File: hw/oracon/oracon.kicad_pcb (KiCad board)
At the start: 2 copper layers, 81 x 56 mm, 108 parts, among them J2 SIM_Card, J3 USB_A, J4 Conn_Coaxial, J5 USB_C_Receptacle_USB2.0_16P, Q1 SS8050, Q2 SS8050, Q3 SS8050, Q5 SS8050, SW1 SW_Push, U1 TP5100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

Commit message: Further routing
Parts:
- moved R10 1.75 mm to (3.42, 101.1)
- moved R11 1.75 mm to (2.44, 101.1)
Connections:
- U3 pad 11: unconnected-(U3-IO7-Pad11) -> LED1_B
- U3 pad 12: unconnected-(U3-IO8-Pad12) -> LED1_G
- U3 pad 13: unconnected-(U3-IO9-Pad13) -> LED1_R
- U3 pad 16: unconnected-(U3-IO12-Pad16) -> SI_TX
- U3 pad 17: unconnected-(U3-IO13-Pad17) -> SI_RX
- U3 pad 18: SI_TX -> ADC_BATT
- U3 pad 19: SI_RX -> NBIOT_TX
- U3 pad 20: ADC_BATT -> NBIOT_RX
- U3 pad 21: NBIOT_TX -> CHG_STAT
- U3 pad 22: NBIOT_RX -> STBY_STAT
- U3 pad 23: CHG_STAT -> unconnected-(U3-IO19-Pad23)
- U3 pad 24: STBY_STAT -> unconnected-(U3-IO20-Pad24)
- U3 pad 25: LED1_B -> unconnected-(U3-IO21-Pad25)
- U3 pad 26: LED1_G -> unconnected-(U3-IO26-Pad26)
- U3 pad 27: LED1_R -> unconnected-(U3-IO47-Pad27)
- U3 pad 28: LED3_R -> unconnected-(U3-IO33-Pad28)
- U3 pad 29: LED3_G -> unconnected-(U3-IO34-Pad29)
- U3 pad 30: LED3_B -> unconnected-(U3-IO48-Pad30)
- U3 pad 31: LED2_R -> unconnected-(U3-IO35-Pad31)
- U3 pad 32: LED2_G -> unconnected-(U3-IO36-Pad32)
- U3 pad 33: LED2_B -> LED3_R
- U3 pad 34: unconnected-(U3-IO38-Pad34) -> LED3_G
- U3 pad 35: unconnected-(U3-IO39-Pad35) -> LED3_B
- U3 pad 36: unconnected-(U3-IO40-Pad36) -> LED2_R
- U3 pad 37: unconnected-(U3-IO41-Pad37) -> LED2_G
- U3 pad 38: unconnected-(U3-IO42-Pad38) -> LED2_B
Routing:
- net LED1_R: track 49.3 -> 57.2 mm
- net LED3_R: track 29.9 -> 22.6 mm
- net LED1_G: track 49.7 -> 56.0 mm
- net LED3_G: track 28.9 -> 23.0 mm
- net LED2_R: track 47.8 -> 42.6 mm
- net LED1_B: track 50.6 -> 55.4 mm
- net LED3_B: track 27.9 -> 23.5 mm
- net LED2_B: track 47.6 -> 43.2 mm
- net LED2_G: track 47.1 -> 42.7 mm
- net PC_RX: track 38.9 -> 41.5 mm
- net PC_TX: track 40.0 -> 42.1 mm
- net VCC: track 42.6 -> 41.0 mm
- net SI_TX: track 22.0 -> 23.5 mm
- net SI_RX: track 19.3 -> 20.6 mm
- net NBIOT_RX: track 43.6 -> 44.5 mm
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
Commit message: Moved charging LED to green channel
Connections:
- D5 pad 2: unconnected-(D5-GK-Pad2) -> Net-(D5-GK)
- D5 pad 3: Net-(D5-BK) -> unconnected-(D5-BK-Pad3)
- R25 pad 2: Net-(D5-BK) -> Net-(D5-GK)
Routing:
- net Net-(D5-BK): track 3.95 -> 0.00 mm
- net Net-(D5-GK): track 0.00 -> 2.51 mm
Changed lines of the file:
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@@
 	(net 79 "LED3_R")
 	(net 80 "VCC")
-	(net 81 "Net-(D5-BK)")
-	(net 82 "unconnected-(D5-GK-Pad2)")
+	(net 81 "unconnected-(D5-BK-Pad3)")
+	(net 82 "Net-(D5-GK)")
 	(net 83 "Net-(D5-RK)")
 	(net 84 "unconnected-(U3-IO5-Pad9)")
@@
 			(size 1.5 1)
 			(layers "F.Cu" "F.Mask" "F.Paste")
-			(net 82 "unconnected-(D5-GK-Pad2)")
+			(net 82 "Net-(D5-GK)")
 			(pinfunction "GK")
 			(pintype "passive")
@@
 			(size 1.5 1)
 			(layers "F.Cu" "F.Mask" "F.Paste")
-			(net 81 "Net-(D5-BK)")
+			(net 81 "unconnected-(D5-BK-Pad3)")
 			(pinfunction "BK")
 			(pintype "passive")
@@
 			(layers "F.Cu" "F.Mask" "F.Paste")
 			(roundrect_rratio 0.25)
-			(net 81 "Net-(D5-BK)")
+			(net 82 "Net-(D5-GK)")
 			(pintype "passive")
 		)
@@
 		)
 	)
+	(dimension
+		(type orthogonal)
+		(layer "Cmts.User")
+		(pts
+			(xy 44.700001 107.6) (xy 44.700001 51.599999)
+		)
+		(height 15.609999)
+		(orientation 1)
+		(format
+			(prefix "")
+			(suffix "")
+			(units 3)
+			(units_format 1)
+			(precision 4)
+		)
+		(style
+			(thickness 0.1)
+			(arrow_length 1.27)
+			(text_position_mode 0)
+			(arrow_direction outward)
+			(extension_height 0.58642)
+			(extension_offset 0.5)
+			(keep_text_aligned yes)
+		)
+		(gr_text "56,0000 mm"
+			(at 59.16 79.599999 90)
+			(layer "Cmts.User")
+			(effects
+				(font
+					(size 1 1)
+					(thickness 0.15)
+				)
+			)
+		)
+	)
+	(dimension
+		(type orthogonal)
+		(layer "Cmts.User")
+		(pts
+			(xy -9.66 79.74) (xy 44.66 85.02)
+		)
+		(height -38.17)
+		(orientation 0)
+		(format
+			(prefix "")
+			(suffix "")
+			(units 3)
+			(units_format 1)
+			(precision 4)
+		)
+		(style
+			(thickness 0.1)
+			(arrow_length 1.27)
+			(text_position_mode 0)
+			(arrow_direction outward)
+			(extension_height 0.58642)
+			(extension_offset 0.5)
+			(keep_text_aligned yes)
+		)
+		(gr_text "54,3200 mm"
+			(at 17.5 40.42 0)
+			(layer "Cmts.User")
+			(effects
+				(font
+					(size 1 1)
+					(thickness 0.15)
+				)
+			)
+		)
+	)
 	(via
 		(at 24.27 81.58)
@@
 	)
 	(segment
-		(start -31.55 90.5)
-		(end -29.26 92.79)
+		(start -31.54 94.01)
+		(end -31.55 94)
+		(width 0.2)
+		(layer "F.Cu")
+		(net 82)
+	)
+	(segment
+		(start -29.26 93.5)
+		(end -29.77 94.01)
 		(width 0.2)
 		(layer "F.Cu")
-		(net 81)
+		(net 82)
 	)
 	(segment
-		(start -29.26 92.79)
-		(end -29.26 93.5)
+		(start -29.77 94.01)
+		(end -31.54 94.01)
 		(width 0.2)
 		(layer "F.Cu")
-		(net 81)
+		(net 82)
+	)
+	(segment
+		(start -32.849 95.051)
+		(end -32.95 94.95)
+		(width 0.2)
+		(layer "F.Cu")
+		(net 83)
 	)
 	(segment
-		(start -32.95 93.548)
-		(end -32.351 92.949)
+		(start -32.95 94.95)
+		(end -32.95 94)
 		(width 0.2)
 		(layer "F.Cu")
@@
 	)
 	(segment
-		(start -32.351 92.949)
-		(end -30.801 92.949)
+		(start -29.801 95.051)
+		(end -32.849 95.051)
 		(width 0.2)
 		(layer "F.Cu")
@@
 	)
 	(segment
-		(start -30.801 92.949)
-		(end -29.25 94.5)
+		(start -29.25 94.5)
+		(end -29.801 95.051)
 		(width 0.2)
 		(layer "F.Cu")

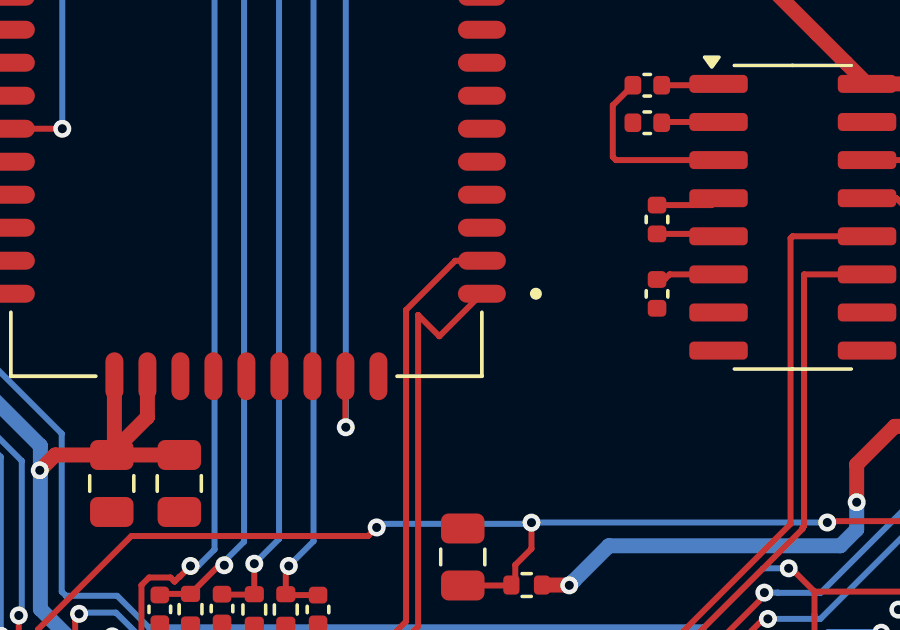
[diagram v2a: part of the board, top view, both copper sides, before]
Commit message: Unconnected schema fix
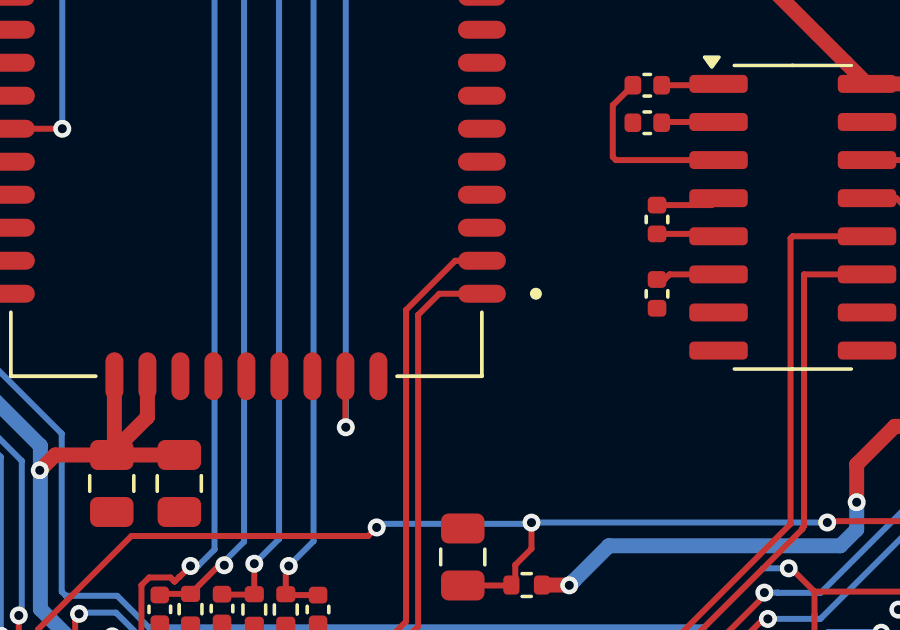
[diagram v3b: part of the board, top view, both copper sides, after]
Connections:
- U7 pad 12: Net-(U7-~{WAKEUP}-Pad12) -> unconnected-(U7-~{WAKEUP}-Pad12)_1
- U7 pad 39: Net-(U7-~{WAKEUP}-Pad12) -> unconnected-(U7-~{WAKEUP}-Pad12)
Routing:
- net NBIOT_RX: track 44.5 -> 44.0 mm
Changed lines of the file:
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@@
 	(net 102 "unconnected-(U7-RESERVED-Pad9)")
 	(net 103 "unconnected-(U7-UART0_RXD-Pad23)")
-	(net 104 "Net-(U7-~{WAKEUP}-Pad12)")
+	(net 104 "unconnected-(U7-~{WAKEUP}-Pad12)")
 	(net 105 "unconnected-(U7-UART1_DCD-Pad5)")
 	(net 106 "Net-(Q3-C)")
@@
 	(net 132 "unconnected-(U3-IO20-Pad24)")
 	(net 133 "unconnected-(U3-IO19-Pad23)")
+	(net 134 "unconnected-(U7-~{WAKEUP}-Pad12)_1")
 	(footprint "TestPoint:TestPoint_Pad_D1.5mm"
 		(layer "F.Cu")
@@
 			(net 12 "unconnected-(J5-SBU1-PadA8)")
 			(pinfunction "SBU1")
-			(pintype "bidirectional")
+			(pintype "bidirectional+no_connect")
 		)
 		(pad "B5" smd rect
@@
 			(net 11 "unconnected-(J5-SBU2-PadB8)")
 			(pinfunction "SBU2")
-			(pintype "bidirectional")
+			(pintype "bidirectional+no_connect")
 		)
 		(pad "S1" thru_hole oval
@@
 			(net 96 "unconnected-(J2-VPP-Pad6)")
 			(pinfunction "VPP")
-			(pintype "input")
+			(pintype "input+no_connect")
 			(thermal_bridge_angle 45)
 		)
@@
 			(net 97 "unconnected-(U7-UART1_RTS-Pad3)")
 			(pinfunction "UART1_RTS")
-			(pintype "input")
+			(pintype "input+no_connect")
 			(solder_mask_margin 0.102)
 		)
@@
 			(net 92 "unconnected-(U7-UART1_CTS-Pad4)")
 			(pinfunction "UART1_CTS")
-			(pintype "output")
+			(pintype "output+no_connect")
 			(solder_mask_margin 0.102)
 		)
@@
 			(net 105 "unconnected-(U7-UART1_DCD-Pad5)")
 			(pinfunction "UART1_DCD")
-			(pintype "output")
+			(pintype "output+no_connect")
 			(solder_mask_margin 0.102)
 		)
@@
 			(net 88 "unconnected-(U7-UART1_DTR-Pad6)")
 			(pinfunction "UART1_DTR")
-			(pintype "input")
+			(pintype "input+no_connect")
 			(solder_mask_margin 0.102)
 		)
@@
 			(net 94 "unconnected-(U7-UART1_RI-Pad7)")
 			(pinfunction "UART1_RI")
-			(pintype "output")
+			(pintype "output+no_connect")
 			(solder_mask_margin 0.102)
 		)
@@
 			(net 108 "unconnected-(U7-BOOT-Pad10)")
 			(pinfunction "BOOT")
-			(pintype "input")
+			(pintype "input+no_connect")
 			(solder_mask_margin 0.102)
 		)
@@
 			(net 109 "unconnected-(U7-AON_GPIO-Pad11)")
 			(pinfunction "AON_GPIO")
-			(pintype "bidirectional")
+			(pintype "bidirectional+no_connect")
 			(solder_mask_margin 0.102)
 		)
@@
 			(size 1.6 0.6)
 			(layers "F.Cu" "F.Mask" "F.Paste")
-			(net 104 "Net-(U7-~{WAKEUP}-Pad12)")
+			(net 134 "unconnected-(U7-~{WAKEUP}-Pad12)_1")
 			(pinfunction "~{WAKEUP}")
-			(pintype "input")
+			(pintype "input+no_connect")
 			(solder_mask_margin 0.102)
 		)
@@
 			(net 110 "unconnected-(U7-GPIO1-Pad14)")
 			(pinfunction "GPIO1")
-			(pintype "bidirectional")
+			(pintype "bidirectional+no_connect")
 			(solder_mask_margin 0.102)
 		)
@@
 			(net 90 "unconnected-(U7-UART0_TXD-Pad22)")
 			(pinfunction "UART0_TXD")
-			(pintype "output")
+			(pintype "output+no_connect")
 			(solder_mask_margin 0.102)
 		)
@@
 			(net 103 "unconnected-(U7-UART0_RXD-Pad23)")
 			(pinfunction "UART0_RXD")
-			(pintype "input")
+			(pintype "input+no_connect")
 			(solder_mask_margin 0.102)
 		)
@@
 			(net 87 "unconnected-(U7-GPIO2-Pad29)")
 			(pinfunction "GPIO2")
-			(pintype "bidirectional")
+			(pintype "bidirectional+no_connect")
 			(solder_mask_margin 0.102)
 		)
@@
 			(net 107 "unconnected-(U7-ADC-Pad38)")
 			(pinfunction "ADC")
-			(pintype "input")
+			(pintype "input+no_connect")
 			(solder_mask_margin 0.102)
 		)
@@
 			(size 0.6 1.6)
 			(layers "F.Cu" "F.Mask" "F.Paste")
-			(net 104 "Net-(U7-~{WAKEUP}-Pad12)")
+			(net 104 "unconnected-(U7-~{WAKEUP}-Pad12)")
 			(pinfunction "~{WAKEUP}")
-			(pintype "input")
+			(pintype "input+no_connect")
 			(solder_mask_margin 0.102)
 		)
@@
 			(net 91 "unconnected-(U7-VDD_EXT-Pad40)")
 			(pinfunction "VDD_EXT")
-			(pintype "power_in")
+			(pintype "power_in+no_connect")
 			(solder_mask_margin 0.102)
 		)
@@
 			(net 111 "unconnected-(U7-STATUS-Pad42)")
 			(pinfunction "STATUS")
-			(pintype "output")
+			(pintype "output+no_connect")
 			(solder_mask_margin 0.102)
 		)
@@
 			(net 81 "unconnected-(D5-BK-Pad3)")
 			(pinfunction "BK")
-			(pintype "passive")
+			(pintype "passive+no_connect")
 		)
 		(pad "4" smd rect
@@
 			(net 36 "unconnected-(U4-~{ACT}-Pad10)")
 			(pinfunction "~{ACT}")
-			(pintype "output")
+			(pintype "output+no_connect")
 		)
 		(pad "11" smd roundrect
@@
 			(net 34 "unconnected-(U4-~{DCD}-Pad11)")
 			(pinfunction "~{DCD}")
-			(pintype "input")
+			(pintype "input+no_connect")
 		)
 		(pad "12" smd roundrect
@@
 			(net 35 "unconnected-(U4-~{DSR}-Pad14)")
 			(pinfunction "~{DSR}")
-			(pintype "input")
+			(pintype "input+no_connect")
 		)
 		(pad "15" smd roundrect
@@
 			(net 38 "unconnected-(U4-~{CTS}-Pad15)")
 			(pinfunction "~{CTS}")
-			(pintype "input")
+			(pintype "input+no_connect")
 		)
 		(pad "16" smd roundrect
@@
 			(net 37 "unconnected-(U4-~{RI}-Pad16)")
 			(pinfunction "~{RI}")
-			(pintype "input")
+			(pintype "input+no_connect")
 		)
 		(pad "17" smd rect
@@
 			(net 52 "unconnected-(U6-T2OUT-Pad7)")
 			(pinfunction "T2OUT")
-			(pintype "output")
+			(pintype "output+no_connect")
 		)
 		(pad "8" smd roundrect
@@
 			(net 54 "unconnected-(U6-R2IN-Pad8)")
 			(pinfunction "R2IN")
-			(pintype "input")
+			(pintype "input+no_connect")
 		)
 		(pad "9" smd roundrect
@@
 			(net 51 "unconnected-(U6-R2OUT-Pad9)")
 			(pinfunction "R2OUT")
-			(pintype "output")
+			(pintype "output+no_connect")
 		)
 		(pad "10" smd roundrect
@@
 			(net 53 "unconnected-(U6-T2IN-Pad10)")
 			(pinfunction "T2IN")
-			(pintype "input")
+			(pintype "input+no_connect")
 		)
 		(pad "11" smd roundrect
@@
 			(net 84 "unconnected-(U3-IO5-Pad9)")
 			(pinfunction "IO5")
-			(pintype "bidirectional")
+			(pintype "bidirectional+no_connect")
 		)
 		(pad "10" smd rect
@@
 			(net 85 "unconnected-(U3-IO6-Pad10)")
 			(pinfunction "IO6")
-			(pintype "bidirectional")
+			(pintype "bidirectional+no_connect")
 		)
 		(pad "11" smd rect
@@
 			(net 28 "unconnected-(U3-IO10-Pad14)")
 			(pinfunction "IO10")
-			(pintype "bidirectional")
+			(pintype "bidirectional+no_connect")
 		)
 		(pad "15" smd rect
@@
 			(net 24 "unconnected-(U3-IO11-Pad15)")
 			(pinfunction "IO11")
-			(pintype "bidirectional")
+			(pintype "bidirectional+no_connect")
 		)
 		(pad "16" smd rect
@@
 			(net 133 "unconnected-(U3-IO19-Pad23)")
 			(pinfunction "IO19")
-			(pintype "bidirectional")
+			(pintype "bidirectional+no_connect")
 		)
 		(pad "24" smd rect
@@
 			(net 132 "unconnected-(U3-IO20-Pad24)")
 			(pinfunction "IO20")
-			(pintype "bidirectional")
+			(pintype "bidirectional+no_connect")
 		)
 		(pad "25" smd rect
@@
 			(net 130 "unconnected-(U3-IO21-Pad25)")
 			(pinfunction "IO21")
-			(pintype "bidirectional")
+			(pintype "bidirectional+no_connect")
 		)
 		(pad "26" smd rect
@@
 			(net 131 "unconnected-(U3-IO26-Pad26)")
 			(pinfunction "IO26")
-			(pintype "bidirectional")
+			(pintype "bidirectional+no_connect")
 		)
 		(pad "27" smd rect
@@
 			(net 129 "unconnected-(U3-IO47-Pad27)")
 			(pinfunction "IO47")
-			(pintype "bidirectional")
+			(pintype "bidirectional+no_connect")
 		)
 		(pad "28" smd rect
@@
 			(net 127 "unconnected-(U3-IO33-Pad28)")
 			(pinfunction "IO33")
-			(pintype "bidirectional")
+			(pintype "bidirectional+no_connect")
 		)
 		(pad "29" smd rect
@@
 			(net 126 "unconnected-(U3-IO34-Pad29)")
 			(pinfunction "IO34")
-			(pintype "bidirectional")
+			(pintype "bidirectional+no_connect")
 		)
 		(pad "30" smd rect
@@
 			(net 128 "unconnected-(U3-IO48-Pad30)")
 			(pinfunction "IO48")
-			(pintype "bidirectional")
+			(pintype "bidirectional+no_connect")
 		)
 		(pad "31" smd rect
@@
 			(net 123 "unconnected-(U3-IO35-Pad31)")
 			(pinfunction "IO35")
-			(pintype "bidirectional")
+			(pintype "bidirectional+no_connect")
 		)
 		(pad "32" smd rect
@@
 			(net 122 "unconnected-(U3-IO36-Pad32)")
 			(pinfunction "IO36")
-			(pintype "bidirectional")
+			(pintype "bidirectional+no_connect")
 		)
 		(pad "33" smd rect
@@
 			(net 26 "unconnected-(U3-IO45-Pad41)")
 			(pinfunction "IO45")
-			(pintype "bidirectional")
+			(pintype "bidirectional+no_connect")
 		)
 		(pad "42" smd rect
@@
 			(net 29 "unconnected-(U3-IO46-Pad44)")
 			(pinfunction "IO46")
-			(pintype "bidirectional")
+			(pintype "bidirectional+no_connect")
 		)
 		(pad "45" smd rect
@@
 	)
 	(segment
-		(start 4.490941 85.909059)
-		(end 8.26 82.14)
+		(start 2.15 102.575)
+		(end 4.490941 100.234059)
 		(width 0.2)
 		(layer "F.Cu")
@@
 	)
 	(segment
-		(start 2.15 102.575)
-		(end 4.490941 100.234059)
+		(start 8.26 71.758)
+		(end 8.968 71.05)
 		(width 0.2)
 		(layer "F.Cu")
@@
 	)
 	(segment
-		(start 4.490941 100.234059)
-		(end 4.490941 85.909059)
+		(start -1.054 102.575)
+		(end 2.15 102.575)
 		(width 0.2)
 		(layer "F.Cu")
@@
 	)
 	(segment
-		(start -1.696033 101.704603)
-		(end -1.6 101.800636)
+		(start 4.490941 100.234059)
+		(end 4.490941 85.909059)
 		(width 0.2)
 		(layer "F.Cu")
@@
 	)
 	(segment
-		(start 8.96975 72.46775)
-		(end 10.3875 71.05)
+		(start -1.6 102.029)
+		(end -1.054 102.575)
 		(width 0.2)
 		(layer "F.Cu")
@@
 	)
 	(segment
-		(start 8.26 82.14)
-		(end 8.26 71.758)
+		(start -1.6 101.800636)
+		(end -1.6 102.029)
 		(width 0.2)
 		(layer "F.Cu")
@@
 	)
 	(segment
-		(start -1.6 101.800636)
-		(end -1.6 102.029)
+		(start 8.968 71.05)
+		(end 10.3875 71.05)
 		(width 0.2)
 		(layer "F.Cu")
@@
 	)
 	(segment
-		(start -1.6 102.029)
-		(end -1.054 102.575)
+		(start 4.490941 85.909059)
+		(end 8.26 82.14)
 		(width 0.2)
 		(layer "F.Cu")
@@
 	)
 	(segment
-		(start 8.26 71.758)
-		(end 8.96975 72.46775)
+		(start 8.26 82.14)
+		(end 8.26 71.758)
 		(width 0.2)
 		(layer "F.Cu")
@@
 	)
 	(segment
-		(start -1.054 102.575)
-		(end 2.15 102.575)
+		(start -1.696033 101.704603)
+		(end -1.6 101.800636)
 		(width 0.2)
 		(layer "F.Cu")

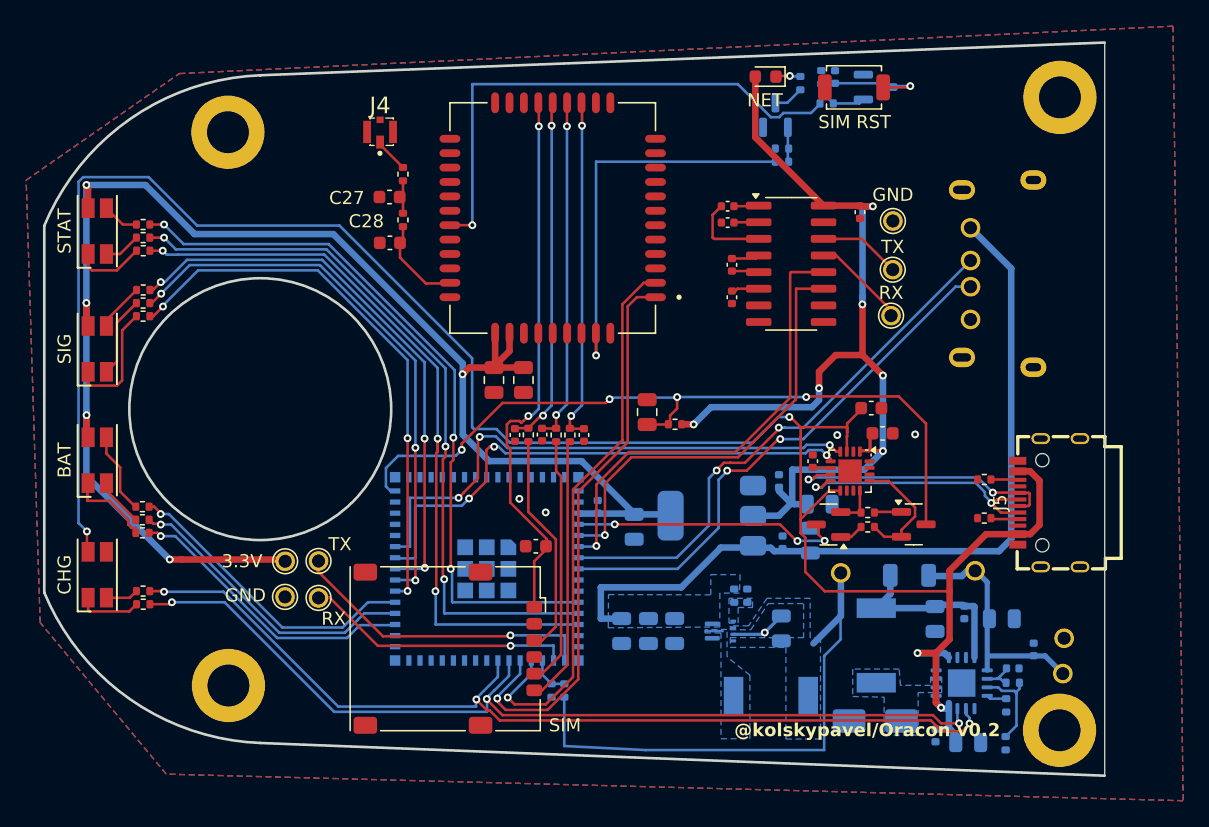
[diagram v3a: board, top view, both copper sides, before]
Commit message: Changed to 4 layer PCB
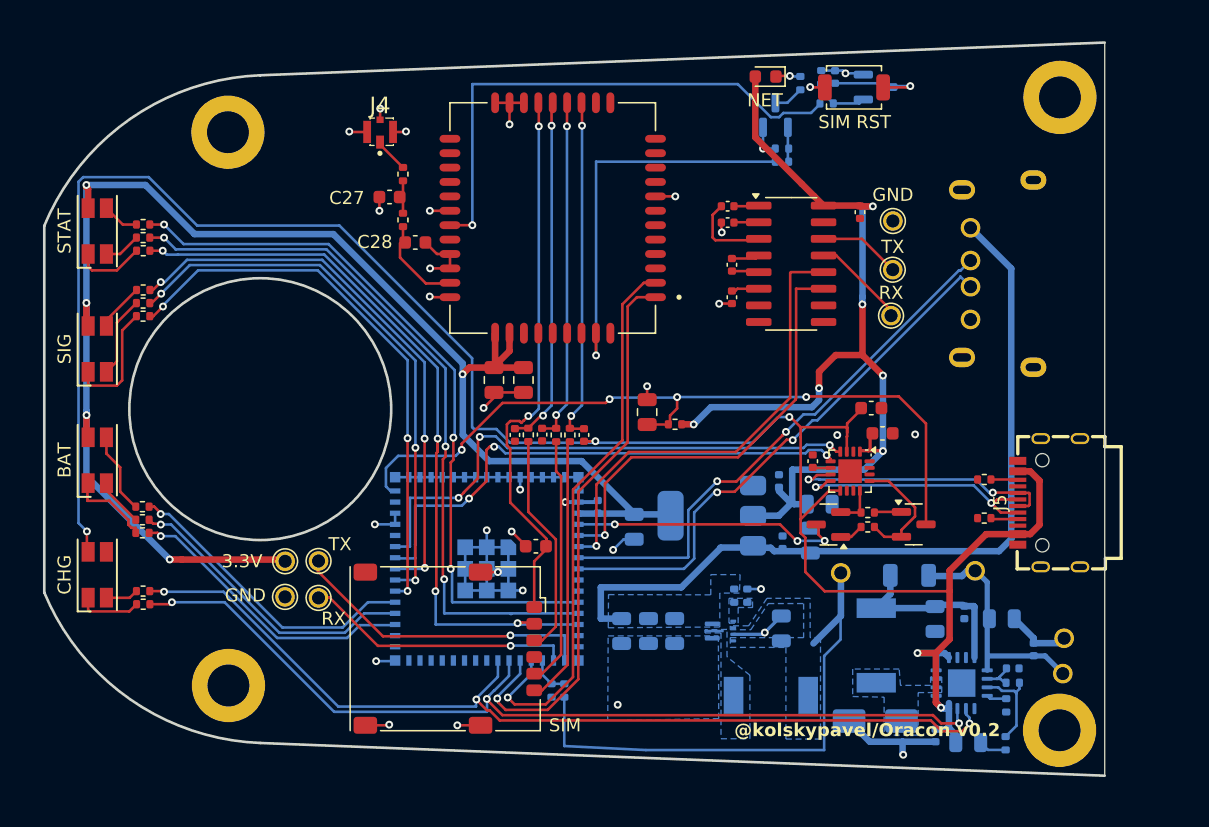
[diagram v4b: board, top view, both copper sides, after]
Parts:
- moved C28 1.94 mm to (-7.96, 66.9), turned to 0 degrees
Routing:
- net GND: track 4.25 -> 108.2 mm, vias 5 -> 35
- net USB_SI_P: track 41.1 -> 41.6 mm
- added copper zone on In1.Cu, net GND
- added copper zone on In2.Cu, net GND
- removed copper zone on F.Cu, net GND
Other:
- copper layers 2 -> 4

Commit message: Finished work with GND
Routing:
- net GND: track 108.2 -> 162.7 mm, vias 35 -> 56
- removed copper zone on B.Cu, net GND
